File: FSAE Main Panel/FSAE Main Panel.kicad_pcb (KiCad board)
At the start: 2 copper layers, 160 x 55 mm, 126 parts, among them J201 USB Micro B, J202 Cortex_Debug, J203 Conn_01x04, J204 TE_84953-6_FPC, Q301 IRLML6402TRPBF, SW1 B3W-1020, SW2 B3W-1020, U1 SAMD21G18A-AU, U301 ZLDO1117-5V, U302 LP2985-3.3, U303 LM1085-5.0, U401 MCP2515-I/ST, U402 MCP2551-I/SN, U501 TLC6C598, U502 TLC6C5816, U503 TLC6C5816, U504 TLC6C5816, Y101 32.768kHz, Y401 Resonator

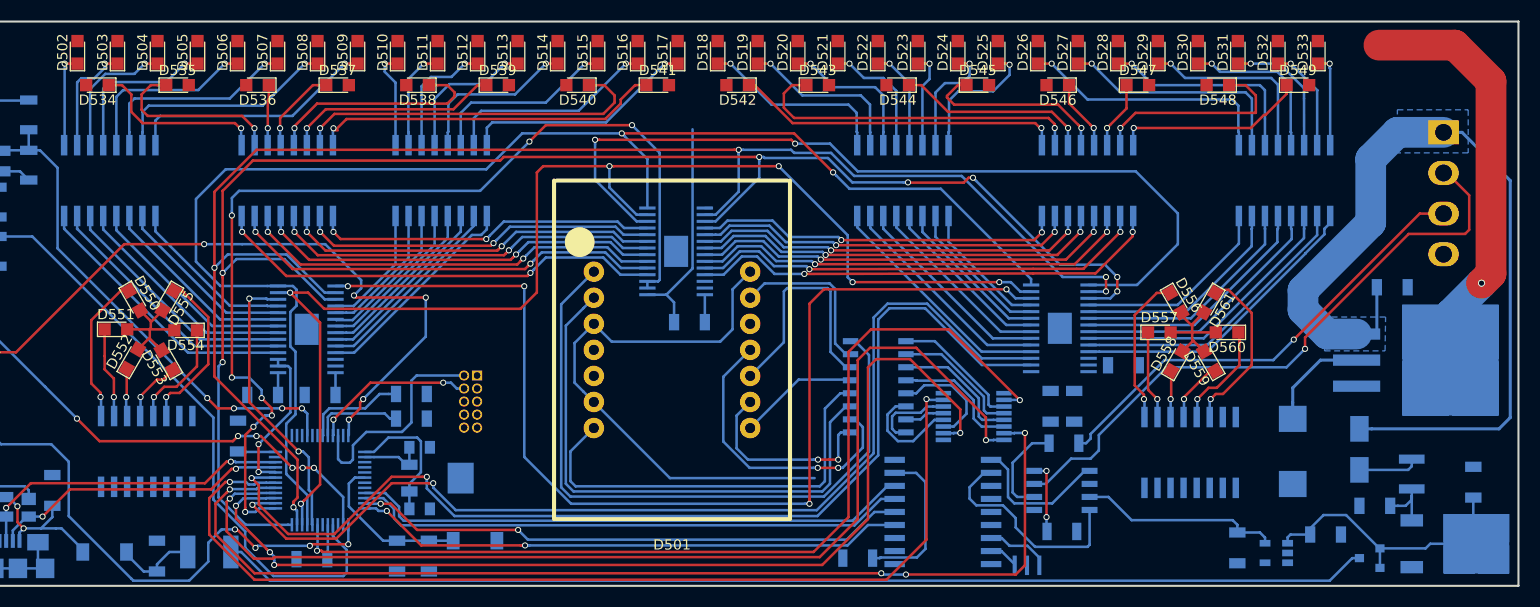
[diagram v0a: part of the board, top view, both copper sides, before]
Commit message: Added warning nMOS circuit, simulated, updated PCB
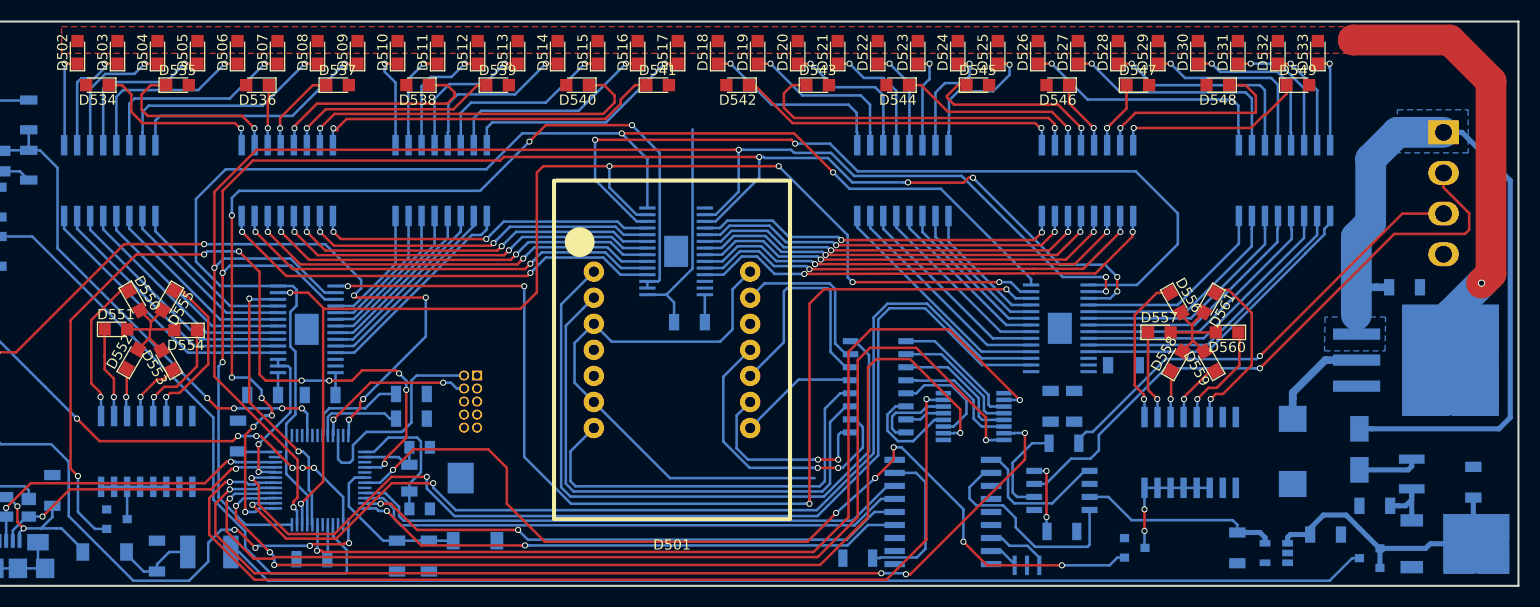
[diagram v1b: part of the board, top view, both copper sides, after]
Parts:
- added Q501: SI2308CDS-T1-GE3, TO_SOT_Packages_SMD:SOT-23, B.Cu at (108.4, 82.0)
- added Q502: SI2308CDS-T1-GE3, TO_SOT_Packages_SMD:SOT-23, B.Cu at (207.6, 84.8)
- moved C302 1.20 mm to (233.9, 59.4)
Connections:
- D501 pad 12: (no net) -> Net-(D501-Pad12)
- D501 pad 4: (no net) -> Net-(D501-Pad4)
- D501 pad 5: (no net) -> Net-(D501-Pad5)
- D550 pad 2: Net-(D550-Pad2) -> DWC_+5V
- D551 pad 2: Net-(D550-Pad2) -> DWC_+5V
- D552 pad 2: Net-(D550-Pad2) -> DWC_+5V
- D553 pad 2: Net-(D550-Pad2) -> DWC_+5V
- D554 pad 2: Net-(D550-Pad2) -> DWC_+5V
- D555 pad 2: Net-(D550-Pad2) -> DWC_+5V
- D556 pad 2: Net-(D556-Pad2) -> DWC_+5V
- D557 pad 2: Net-(D556-Pad2) -> DWC_+5V
- D558 pad 2: Net-(D556-Pad2) -> DWC_+5V
- D559 pad 2: Net-(D556-Pad2) -> DWC_+5V
- D560 pad 2: Net-(D556-Pad2) -> DWC_+5V
- D561 pad 2: Net-(D556-Pad2) -> DWC_+5V
- J202 pad 10: (no net) -> Net-(J202-Pad10)
- J202 pad 6: (no net) -> Net-(J202-Pad6)
- J202 pad 7: (no net) -> Net-(J202-Pad7)
- J202 pad 8: (no net) -> Net-(J202-Pad8)
- J202 pad 9: (no net) -> Net-(J202-Pad9)
- R401 pad 2: Net-(U401-Pad2) -> Net-(R401-Pad2)
- RN508 pad 1: (no net) -> Net-(RN508-Pad1)
- RN508 pad 15: (no net) -> Net-(RN508-Pad15)
- RN508 pad 16: (no net) -> Net-(RN508-Pad16)
- RN508 pad 2: (no net) -> Net-(RN508-Pad2)
- RN508 pad 3: Net-(RN508-Pad3) -> Net-(Q501-Pad3)
- RN508 pad 4: Net-(RN508-Pad4) -> Net-(Q501-Pad3)
- RN508 pad 5: Net-(RN508-Pad5) -> Net-(Q501-Pad3)
- RN508 pad 6: Net-(RN508-Pad6) -> Net-(Q501-Pad3)
- RN508 pad 7: Net-(RN508-Pad7) -> Net-(Q501-Pad3)
- RN508 pad 8: Net-(RN508-Pad8) -> Net-(Q501-Pad3)
- RN509 pad 1: (no net) -> Net-(RN509-Pad1)
- RN509 pad 15: (no net) -> Net-(RN509-Pad15)
- RN509 pad 16: (no net) -> Net-(RN509-Pad16)
- RN509 pad 2: (no net) -> Net-(RN509-Pad2)
- RN509 pad 3: Net-(RN509-Pad3) -> Net-(Q502-Pad3)
- RN509 pad 4: Net-(RN509-Pad4) -> Net-(Q502-Pad3)
- RN509 pad 5: Net-(RN509-Pad5) -> Net-(Q502-Pad3)
- RN509 pad 6: Net-(RN509-Pad6) -> Net-(Q502-Pad3)
- RN509 pad 7: Net-(RN509-Pad7) -> Net-(Q502-Pad3)
- RN509 pad 8: Net-(RN509-Pad8) -> Net-(Q502-Pad3)
- U1 pad 11: CAN_MOSI -> CAN_CS
- U1 pad 25: /Display/~G5 -> /~G5
- U1 pad 26: /Display/~G4 -> /~G4
- U1 pad 31: /Display/~G3 -> /~G3
- U1 pad 32: /Display/~G1 -> /~G1
- U1 pad 4: Net-(U1-Pad4) -> HIGH_TEMP
- U1 pad 7: Net-(U1-Pad7) -> OIL_PRES
- U1 pad 9: CAN_CS -> CAN_MOSI
- U302 pad 3: (no net) -> Net-(U302-Pad3)
- U302 pad 4: (no net) -> Net-(U302-Pad4)
- U401 pad 10: (no net) -> Net-(U401-Pad10)
- U401 pad 11: (no net) -> Net-(U401-Pad11)
- U401 pad 12: (no net) -> Net-(U401-Pad12)
- U401 pad 17: Net-(U401-Pad2) -> Net-(R401-Pad2)
- U401 pad 3: (no net) -> Net-(U401-Pad3)
- U401 pad 4: (no net) -> Net-(U401-Pad4)
- U401 pad 5: (no net) -> Net-(U401-Pad5)
- U401 pad 6: (no net) -> Net-(U401-Pad6)
- U402 pad 5: (no net) -> Net-(U402-Pad5)
- U501 pad 9: (no net) -> Net-(U501-Pad9)
- U502 pad 26: (no net) -> Net-(U502-Pad26)
- U502 pad 27: (no net) -> Net-(U502-Pad27)
- U502 pad 3: /Display/~G1 -> /Display/~G2
- U503 pad 26: (no net) -> Net-(U503-Pad26)
- U503 pad 27: (no net) -> Net-(U503-Pad27)
- U504 pad 15: (no net) -> GEAR_IN
- U504 pad 26: (no net) -> Net-(U504-Pad26)
- U504 pad 27: (no net) -> Net-(U504-Pad27)
- U504 pad 3: /Display/~G5 -> /Display/~G6
- Y101 pad 3: GND -> (no net)
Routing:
- net OIL_PRES: track 0.00 -> 92.5 mm, vias 0 -> 6
- net HIGH_TEMP: track 0.00 -> 80.9 mm, vias 0 -> 8
- net DWC_+5V: track 11.9 -> 79.3 mm, vias 0 -> 1
- net (no net): track 41.8 -> 0.00 mm, vias 1 -> 0
- net Net-(R401-Pad2): track 0.00 -> 15.4 mm
- net Net-(U401-Pad2): track 37.8 -> 22.4 mm
- net Net-(D550-Pad2): track 12.7 -> 0.00 mm
- net Net-(D556-Pad2): track 12.6 -> 0.00 mm
- net Net-(Q502-Pad3): track 0.00 -> 12.2 mm, vias 0 -> 2
- net Net-(Q501-Pad3): track 0.00 -> 9.51 mm
- net CAN_V+: track 84.9 -> 76.8 mm
- net GEAR_CLR: track 105.3 -> 99.3 mm
- net RPM_CLR: track 125.6 -> 123.0 mm
- net CAN_H: track 61.5 -> 60.7 mm
- net GEAR_IN: track 93.9 -> 94.6 mm
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- added copper zone on F.Cu, net DWC_+5V

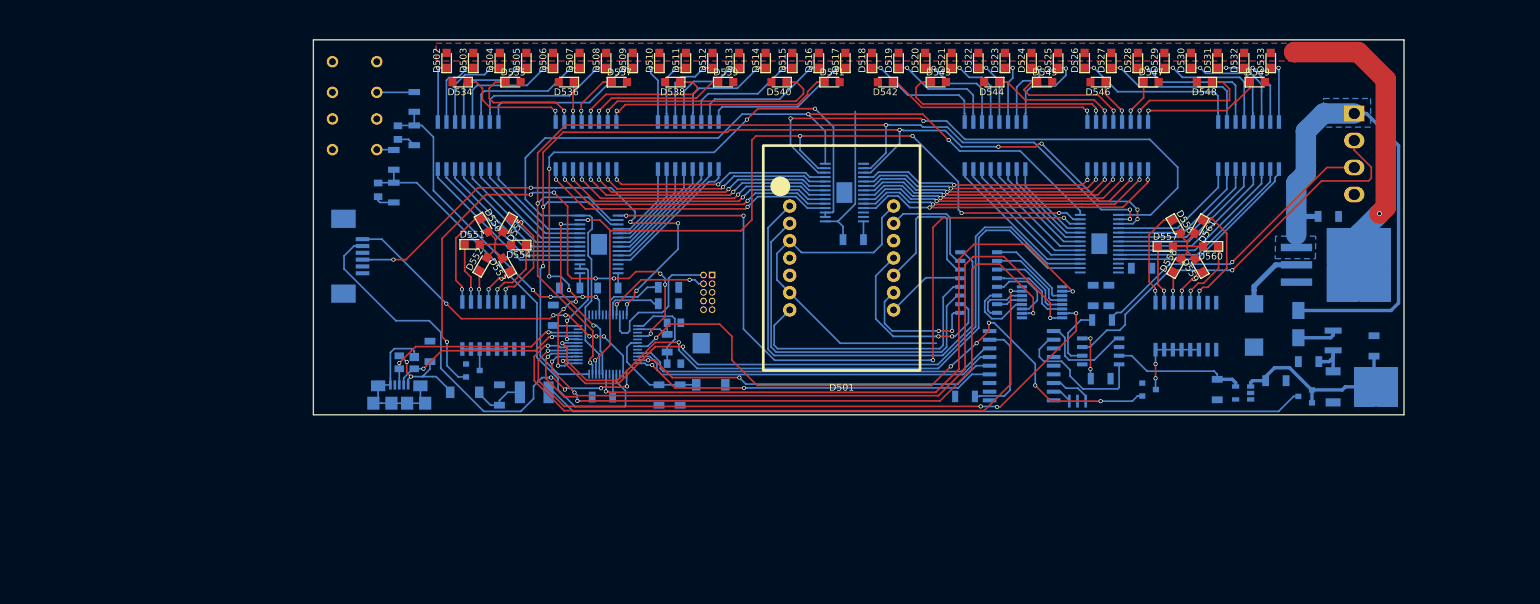
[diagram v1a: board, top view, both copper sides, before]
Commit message: Major Revision
Deleted a ton of routes, Sorry Gary.
Changed all LEDs to 1206s for better brightness
Added a lot of local net names for easier routing
Flipped J203 for better routing
Expanded board outline to fit final dashboard cutout
Added half of the Mounting Holes
Realigned RPM strip
Added Linear Reg Load Resistors to meet minimum current specs
Changed Aux load Linear Regulators to a better one
Added Separate Linear Reg for the DWC
Tuned the CAN Bus differential Pair Lines for equal length
Added decoupling capacitors at a few locations
Rerouted Power traces to be shorter and cleaner
Set up keep out zones for CAN bus interference shielding.
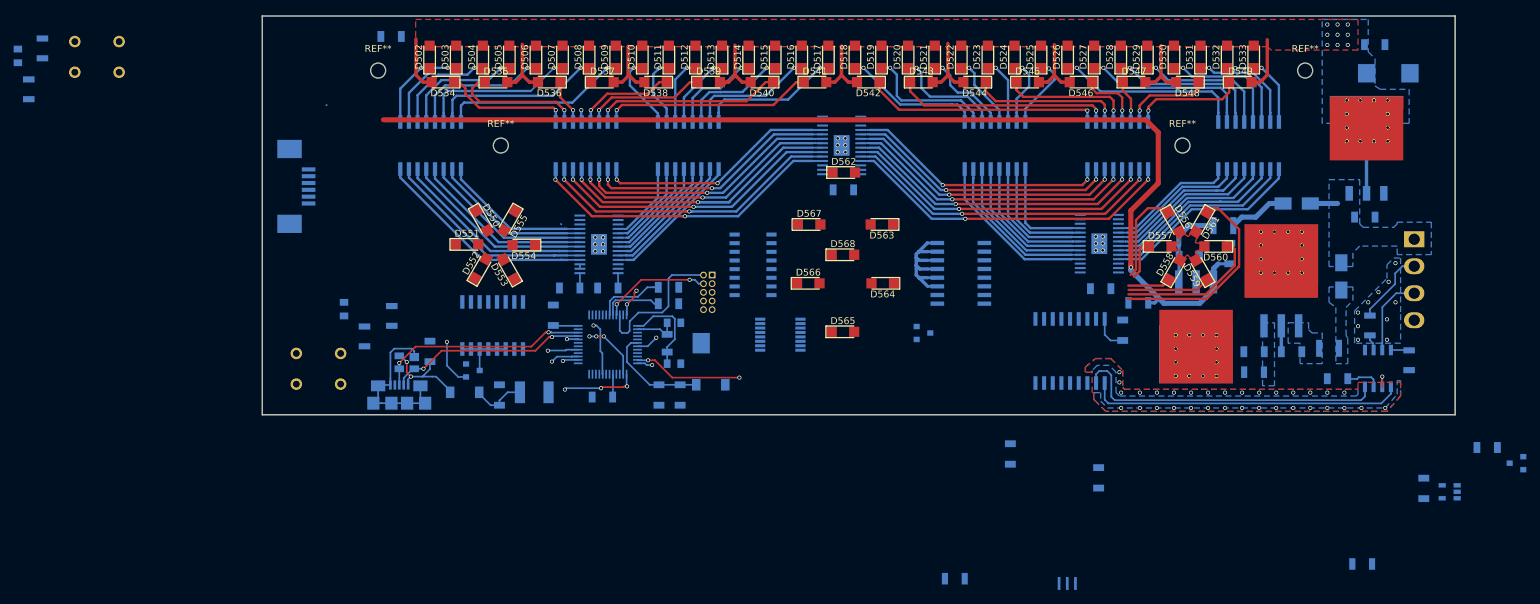
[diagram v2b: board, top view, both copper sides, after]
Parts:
- removed D501: SA10-11GWA, Kingbright:SC10-11EWA
- added C307: 1uF, Capacitors_SMD:C_1206, B.Cu at (213.5, 65.2)
- added C308: 100nF, Capacitors_SMD:C_1206, B.Cu at (219.4, 64.8)
- added C309: 47uF, Capacitors_SMD:C_1206, B.Cu at (240.7, 34.2)
- added C401: 100nF, Capacitors_SMD:C_1206, B.Cu at (235.2, 83.2)
- added C402: 100nF, Capacitors_SMD:C_1206, B.Cu at (203.7, 76.1)
- added C507: 47uF, Capacitors_SMD:C_1206, B.Cu at (96.4, 33.0)
- added D302: BYS10-45-E3/TR, Diodes_SMD:D_SMA, B.Cu at (229.2, 57.5)
- added D562: LG R971, LEDs:LED_1206, F.Cu at (162.8, 53.0)
- added D563: LG R971, LEDs:LED_1206, F.Cu at (168.4, 60.6)
- added D564: LG R971, LEDs:LED_1206, F.Cu at (168.5, 69.2)
- added D565: LG R971, LEDs:LED_1206, F.Cu at (162.7, 76.3)
- added D566: LG R971, LEDs:LED_1206, F.Cu at (157.6, 69.2)
- added D567: LG R971, LEDs:LED_1206, F.Cu at (157.7, 60.6)
- added D568: LG R971, LEDs:LED_1206, F.Cu at (162.7, 65.0)
- added L302: 742792310 Ferrite Bead, Inductors_SMD:L_1210, B.Cu at (218.5, 60.8)
- added R301: 909, Resistors_SMD:R_1206, B.Cu at (223.0, 82.2)
- added R302: 909, Resistors_SMD:R_1206, B.Cu at (238.9, 110.4)
- added R303: 909, Resistors_SMD:R_1206, B.Cu at (206.0, 72.1)
- added REF**: MountingHole_2.2mm_M2, Mounting_Holes:MountingHole_2.2mm_M2, F.Cu at (212.5, 49.0)
- added REF**: MountingHole_2.2mm_M2, Mounting_Holes:MountingHole_2.2mm_M2, F.Cu at (112.5, 49.0)
- added REF**: MountingHole_2.2mm_M2, Mounting_Holes:MountingHole_2.2mm_M2, F.Cu at (94.5, 38.0)
- added REF**: MountingHole_2.2mm_M2, Mounting_Holes:MountingHole_2.2mm_M2, F.Cu at (230.5, 38.0)
- added U304: UA7805CKTTR, Texas_Additions:TO-263-3_TabPin2_PAD_2012, B.Cu at (214.5, 76.5)
- C301: value 4.7uF -> 1uF
- C303: value 4.7uF -> 100nF
- D502, D503, D504, D505, D506, D507, D508, D509, D510, D511, D512, D513, D514, D515, D516, D517, D518, D519, D520, D521, D522, D523, D524, D525, D526, D527, D528, D529, D530, D531, D532, D533, D534, D535, D536, D537, D538, D539, D540, D541, D542, D543, D544, D545, D546, D547, D548, D549, D550, D551, D552, D553, D554, D555, D556, D557, D558, D559, D560, D561: footprint LEDs:LED_0805 -> LEDs:LED_1206
- U301: value ZLDO1117-5V -> UA7805CKTTR; footprint TO_SOT_Packages_SMD:TO-252-2 -> Texas_Additions:TO-263-3_TabPin2_PAD_2012
- U303: footprint TO_SOT_Packages_SMD:TO-263-3_TabPin2 -> Texas_Additions:TO-263-3_TabPin2_Tab
- moved R201 57.0 mm to (43.2, 40.8)
- moved C201 56.9 mm to (41.6, 35.9)
- moved R202 55.1 mm to (45.2, 34.8)
- moved R402 45.3 mm to (245.8, 80.5), turned to 270 degrees
- moved C306 41.9 mm to (242.7, 38.4), turned to 0 degrees
- moved U402 40.8 mm to (241.2, 81.7), turned to 90 degrees
- moved R403 39.3 mm to (240.0, 75.4), turned to 270 degrees
- moved U501 38.7 mm to (153.5, 76.8)
- moved SW1 37.9 mm to (50.0, 38.2)
- moved SW2 34.8 mm to (82.5, 84.0)
- moved Q502 34.1 mm to (174.5, 76.5)
- moved RN509 33.9 mm to (180.0, 67.8), turned to 0 degrees
- moved C305 33.6 mm to (247.9, 99.3)
- moved U302 33.6 mm to (251.7, 99.8)
- moved RN501 33.2 mm to (149.5, 66.5)
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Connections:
- net Net-(C101-Pad1) renamed /VDDANA
- net Net-(C104-Pad2) renamed /XOUT
- net Net-(C105-Pad2) renamed /XIN
- net Net-(C108-Pad1) renamed /VCORE1
- net Net-(C204-Pad2) renamed /External Interface/V_USB_1
- net Net-(D301-Pad1) renamed /Power/CAN_D1
- net Net-(D550-Pad1) renamed /Display/HT1
- net Net-(D551-Pad1) renamed /Display/HT2
- net Net-(D552-Pad1) renamed /Display/HT3
- net Net-(D553-Pad1) renamed /Display/HT4
- net Net-(D554-Pad1) renamed /Display/HT5
- net Net-(D555-Pad1) renamed /Display/HT6
- net Net-(D556-Pad1) renamed /Display/OP1
- net Net-(D557-Pad1) renamed /Display/OP2
- net Net-(D558-Pad1) renamed /Display/OP3
- net Net-(D559-Pad1) renamed /Display/OP4
- net Net-(D560-Pad1) renamed /Display/OP5
- net Net-(D561-Pad1) renamed /Display/OP6
- net Net-(Q501-Pad3) renamed /Display/HT_CONTROL
- net Net-(Q502-Pad3) renamed /Display/OP_CONTROL
- net Net-(R202-Pad2) renamed /External Interface/SW1_L
- net Net-(R204-Pad2) renamed /External Interface/SW2_L
- net Net-(R401-Pad2) renamed /CAN/CANRST
- net Net-(R402-Pad1) renamed /CAN/CANRS
- net Net-(R403-Pad2) renamed /CAN/CANL
- net Net-(RN501-Pad1) renamed /Display/aI
- net Net-(RN501-Pad2) renamed /Display/bI
- net Net-(RN501-Pad3) renamed /Display/cI
- net Net-(RN501-Pad4) renamed /Display/dI
- net Net-(RN501-Pad5) renamed /Display/eI
- net Net-(RN501-Pad6) renamed /Display/fI
- net Net-(RN501-Pad7) renamed /Display/gI
- net Net-(U401-Pad1) renamed /CAN/CAN_TX+
- net Net-(U401-Pad2) renamed /CAN/CAN_TX-
- net Net-(U401-Pad7) renamed /CAN/OSC2
- net Net-(U401-Pad8) renamed /CAN/OSC1
- C301 pad 1: Net-(C301-Pad1) -> /Power/REG1_VIN
- C306 pad 1: DWC_+5V -> LED_+5V
- D502 pad 2: DWC_+5V -> LED_+5V
- D503 pad 2: DWC_+5V -> LED_+5V
- D504 pad 2: DWC_+5V -> LED_+5V
- D505 pad 2: DWC_+5V -> LED_+5V
- D506 pad 2: DWC_+5V -> LED_+5V
- D507 pad 2: DWC_+5V -> LED_+5V
- D508 pad 2: DWC_+5V -> LED_+5V
- D509 pad 2: DWC_+5V -> LED_+5V
- D510 pad 2: DWC_+5V -> LED_+5V
- D511 pad 2: DWC_+5V -> LED_+5V
- D512 pad 2: DWC_+5V -> LED_+5V
- D513 pad 2: DWC_+5V -> LED_+5V
- D514 pad 2: DWC_+5V -> LED_+5V
- D515 pad 2: DWC_+5V -> LED_+5V
- D516 pad 2: DWC_+5V -> LED_+5V
- D517 pad 2: DWC_+5V -> LED_+5V
- D518 pad 2: DWC_+5V -> LED_+5V
- D519 pad 2: DWC_+5V -> LED_+5V
- D520 pad 2: DWC_+5V -> LED_+5V
- D521 pad 2: DWC_+5V -> LED_+5V
- D522 pad 2: DWC_+5V -> LED_+5V
- D523 pad 2: DWC_+5V -> LED_+5V
- D524 pad 2: DWC_+5V -> LED_+5V
- D525 pad 2: DWC_+5V -> LED_+5V
- D526 pad 2: DWC_+5V -> LED_+5V
- D527 pad 2: DWC_+5V -> LED_+5V
- D528 pad 2: DWC_+5V -> LED_+5V
- D529 pad 2: DWC_+5V -> LED_+5V
- D530 pad 2: DWC_+5V -> LED_+5V
- D531 pad 2: DWC_+5V -> LED_+5V
- D532 pad 2: DWC_+5V -> LED_+5V
- D533 pad 2: DWC_+5V -> LED_+5V
- D534 pad 2: DWC_+5V -> LED_+5V
- D535 pad 2: DWC_+5V -> LED_+5V
- D536 pad 2: DWC_+5V -> LED_+5V
- D537 pad 2: DWC_+5V -> LED_+5V
- D538 pad 2: DWC_+5V -> LED_+5V
- D539 pad 2: DWC_+5V -> LED_+5V
- D540 pad 2: DWC_+5V -> LED_+5V
- D541 pad 2: DWC_+5V -> LED_+5V
- D542 pad 2: DWC_+5V -> LED_+5V
- D543 pad 2: DWC_+5V -> LED_+5V
- D544 pad 2: DWC_+5V -> LED_+5V
- D545 pad 2: DWC_+5V -> LED_+5V
- D546 pad 2: DWC_+5V -> LED_+5V
- D547 pad 2: DWC_+5V -> LED_+5V
- D548 pad 2: DWC_+5V -> LED_+5V
- D549 pad 2: DWC_+5V -> LED_+5V
- D550 pad 2: DWC_+5V -> LED_+5V
- D551 pad 2: DWC_+5V -> LED_+5V
- D552 pad 2: DWC_+5V -> LED_+5V
- D553 pad 2: DWC_+5V -> LED_+5V
- D554 pad 2: DWC_+5V -> LED_+5V
- D555 pad 2: DWC_+5V -> LED_+5V
- D556 pad 2: DWC_+5V -> LED_+5V
- D557 pad 2: DWC_+5V -> LED_+5V
- D558 pad 2: DWC_+5V -> LED_+5V
- D559 pad 2: DWC_+5V -> LED_+5V
- D560 pad 2: DWC_+5V -> LED_+5V
- D561 pad 2: DWC_+5V -> LED_+5V
- J203 pad 2: CAN_H -> CAN_IN-
- J203 pad 3: CAN_L -> CAN_IN+
- L301 pad 1: Net-(C301-Pad1) -> /Power/REG1_VIN
- R403 pad 1: CAN_L -> CAN_IN-
- RN501 pad 9: /Display/dp -> Net-(RN501-Pad9)
- U301 pad 1: GND -> /Power/REG1_VIN
- U301 pad 2: +5V -> GND
- U301 pad 3: Net-(C301-Pad1) -> +5V
- U303 pad 2: DWC_+5V -> LED_+5V
- U402 pad 7: CAN_H -> CAN_IN+
- U501 pad 14: Net-(RN501-Pad8) -> Net-(U501-Pad14)
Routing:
- net RPM_SCLK: track 158.3 -> 0.00 mm, vias 7 -> 0
- net RPM_RCLK: track 154.8 -> 0.00 mm, vias 5 -> 0
- net ~RPM_EN: track 140.4 -> 0.00 mm, vias 2 -> 0
- net RPM_CLR: track 123.0 -> 0.00 mm, vias 6 -> 0
- net USB_POWER: track 112.1 -> 0.00 mm
- net ~GEAR_PWM: track 107.4 -> 0.00 mm, vias 2 -> 0
- net Net-(U502-Pad15): track 106.8 -> 0.00 mm, vias 4 -> 0
- net /Display/~G3: track 104.7 -> 0.00 mm, vias 2 -> 0
- net /Display/~G4: track 101.4 -> 0.00 mm, vias 2 -> 0
- net GEAR_SCLK: track 99.5 -> 0.00 mm, vias 2 -> 0
- net /Display/~G5: track 97.8 -> 0.00 mm, vias 8 -> 0
- net GEAR_RCLK: track 101.2 -> 4.16 mm, vias 4 -> 1
- net LED_+5V: track 0.00 -> 96.6 mm, vias 0 -> 9
- net GEAR_CLR: track 99.3 -> 4.51 mm, vias 4 -> 1
- net GEAR_IN: track 94.6 -> 0.00 mm, vias 2 -> 0
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- added copper zone on B.Cu, net +5V
- added copper zone on B.Cu, net /Power/CAN_D1
- added copper zone on B.Cu, net /Power/REG1_VIN
- added copper zone on B.Cu, net GND
- added copper zone on F.Cu, net GND
- added copper zone on B.Cu, net LED_+5V
- added copper zone on F.Cu, net LED_+5V
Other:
- board size 160 x 55 mm -> 175 x 58.5 mm
